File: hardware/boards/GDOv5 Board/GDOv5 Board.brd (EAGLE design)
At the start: 34 x 53.6 mm, 29 parts, among them IC1 DS1820, IC2 3.3V REG, J1 DCJ0202, Q1 BSS84, Q2 BSS138, Q3 BSS138

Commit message: Fixing Board issues
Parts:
- added Q4: IRLML2502, bss138_10:SOT23
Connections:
- new net N$1: J1.3, Q4.3
- net +5V: now also J1.1, Q4.1; no longer J1.3
- net GND: now also Q4.2; no longer J1.1
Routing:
- net +5V: track 49.1 -> 54.1 mm
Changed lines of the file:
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@@
 <layers>
 <layer number="1" name="Top" color="4" fill="1" visible="yes" active="yes"/>
-<layer number="16" name="Bottom" color="1" fill="1" visible="yes" active="yes"/>
+<layer number="16" name="Bottom" color="1" fill="1" visible="no" active="yes"/>
 <layer number="17" name="Pads" color="2" fill="1" visible="yes" active="yes"/>
 <layer number="18" name="Vias" color="2" fill="1" visible="yes" active="yes"/>
@@
 <layer number="20" name="Dimension" color="15" fill="1" visible="yes" active="yes"/>
 <layer number="21" name="tPlace" color="7" fill="1" visible="yes" active="yes"/>
-<layer number="22" name="bPlace" color="7" fill="1" visible="yes" active="yes"/>
+<layer number="22" name="bPlace" color="7" fill="1" visible="no" active="yes"/>
 <layer number="23" name="tOrigins" color="15" fill="1" visible="yes" active="yes"/>
-<layer number="24" name="bOrigins" color="15" fill="1" visible="yes" active="yes"/>
+<layer number="24" name="bOrigins" color="15" fill="1" visible="no" active="yes"/>
 <layer number="25" name="tNames" color="7" fill="1" visible="yes" active="yes"/>
-<layer number="26" name="bNames" color="7" fill="1" visible="yes" active="yes"/>
+<layer number="26" name="bNames" color="7" fill="1" visible="no" active="yes"/>
 <layer number="27" name="tValues" color="7" fill="1" visible="yes" active="yes"/>
 <layer number="28" name="bValues" color="7" fill="1" visible="yes" active="yes"/>
@@
 </element>
 <element name="S1" library="SparkFun-Electromechanical" package="TACTILE-SWITCH-1101NE" value="RESET-SWITCH" x="30.48" y="43.18" rot="R270"/>
+<element name="Q4" library="bss138_10" package="SOT23" value="IRLML2502" x="3.81" y="36.83">
+<attribute name="MPN" value="BSS138" x="3.81" y="36.83" size="1.778" layer="27" display="off"/>
+<attribute name="OC_NEWARK" value="67R2009" x="3.81" y="36.83" size="1.778" layer="27" display="off"/>
+<attribute name="OC_FARNELL" value="9845330" x="3.81" y="36.83" size="1.778" layer="27" display="off"/>
+<attribute name="MF" value="Fairchild" x="3.81" y="36.83" size="1.778" layer="27" display="off"/>
+</element>
 </elements>
 <signals>
@@
 <contactref element="C9" pad="C"/>
 <contactref element="C4" pad="2"/>
-<contactref element="J1" pad="1"/>
 <contactref element="R9" pad="1"/>
 <contactref element="R10" pad="1"/>
@@
 <wire x1="6.4008" y1="76.8096" x2="6.35" y2="76.835" width="0.1524" layer="1"/>
 <via x="9.144" y="52.7304" extent="1-16" drill="0.3302"/>
+<contactref element="Q4" pad="2"/>
+<wire x1="10.795" y1="28.2575" x2="4.76" y2="35.83" width="0" layer="19" extent="1-1"/>
 </signal>
 <signal name="+5V">
 <contactref element="IC2" pad="3"/>
 <contactref element="C8" pad="A"/>
-<contactref element="J1" pad="3"/>
 <wire x1="22.2504" y1="68.7324" x2="24.5364" y2="71.0184" width="0.1524" layer="1"/>
 <wire x1="24.5364" y1="71.0184" x2="24.635" y2="71.12" width="0.1524" layer="1"/>
@@
 <wire x1="2.4384" y1="52.7304" x2="3.6576" y2="53.9496" width="0.1524" layer="1"/>
 <wire x1="2.4384" y1="49.53" x2="2.4384" y2="52.7304" width="0.1524" layer="1"/>
-<wire x1="1.0668" y1="48.1584" x2="2.4384" y2="49.53" width="0.1524" layer="1"/>
-<wire x1="1.0668" y1="43.1292" x2="1.0668" y2="48.1584" width="0.1524" layer="1"/>
-<wire x1="7.0104" y1="37.1856" x2="1.0668" y2="43.1292" width="0.1524" layer="1"/>
 <wire x1="22.098" y1="68.58" x2="22.1996" y2="68.6689" width="0.1524" layer="1"/>
-<wire x1="7.0104" y1="37.1856" x2="7.16" y2="37.1475" width="0.1524" layer="1"/>
+<contactref element="J1" pad="1"/>
+<wire x1="12.54125" y1="37.1475" x2="13.26" y2="37.1475" width="0.1524" layer="1"/>
+<wire x1="2.54" y1="43.33875" x2="12.54125" y2="37.1475" width="0.1524" layer="1"/>
+<wire x1="1.42875" y1="43.33875" x2="2.54" y2="43.33875" width="0.1524" layer="1"/>
+<wire x1="1.11125" y1="43.65625" x2="1.42875" y2="43.33875" width="0.1524" layer="1"/>
+<wire x1="1.11125" y1="48.26" x2="1.11125" y2="43.65625" width="0.1524" layer="1"/>
+<wire x1="2.38125" y1="49.53" x2="1.11125" y2="48.26" width="0.1524" layer="1"/>
+<wire x1="2.38125" y1="49.53" x2="2.4384" y2="49.53" width="0.1524" layer="1"/>
+<contactref element="Q4" pad="1"/>
+<wire x1="2.86" y1="35.83" x2="1.42875" y2="43.33875" width="0" layer="19" extent="1-1"/>
 </signal>
 <signal name="+3.3V">
@@
 <wire x1="21.9456" y1="58.5216" x2="21.91" y2="58.59" width="0.1524" layer="1"/>
 </signal>
+<signal name="N$1">
+<contactref element="J1" pad="3"/>
+<contactref element="Q4" pad="3"/>
+<wire x1="3.81" y1="37.83" x2="7.16" y2="37.1475" width="0" layer="19" extent="1-1"/>
+</signal>
 </signals>

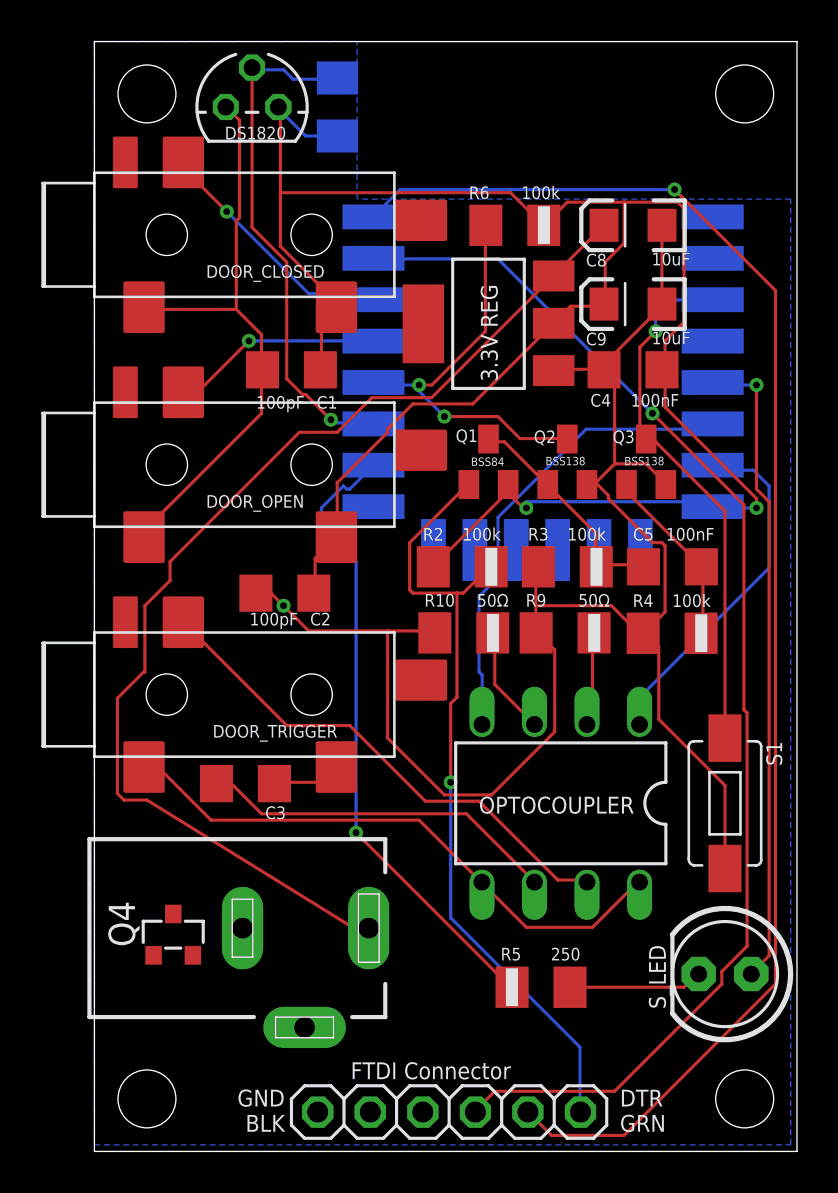
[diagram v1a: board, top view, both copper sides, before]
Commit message: Updating board to better match prototype design
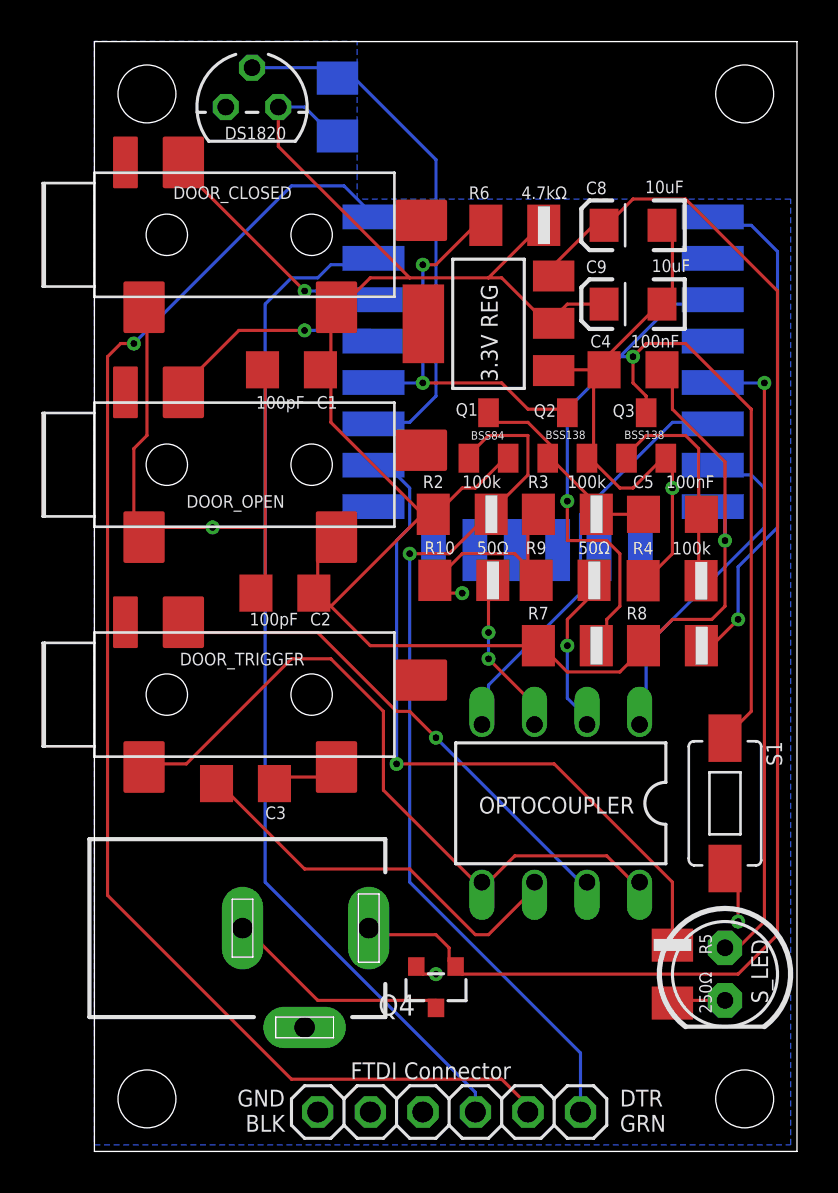
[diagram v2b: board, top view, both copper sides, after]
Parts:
- added R7: 4.7kΩ, resistor:M3216
- added R8: 10k, resistor:M3216
- R5: value 250 -> 250Ω
- R6: value 100k -> 4.7kΩ
- moved Q4 13.0 mm to (16.5, 34.3), turned to 180 degrees
- moved R5 6.38 mm to (27.9, 34.9), turned to 90 degrees
- moved R10 2.54 mm to (17.9, 54.0)
- moved R9 2.54 mm to (22.8, 54.0)
- moved C5 2.54 mm to (27.9, 57.1)
- moved R2 2.54 mm to (17.8, 57.1)
- moved R3 2.54 mm to (22.9, 57.1)
- moved R4 2.54 mm to (27.9, 53.9)
- moved Q1 1.27 mm to (19.1, 61.0)
- moved Q2 1.27 mm to (22.9, 61.0)
- moved Q3 1.27 mm to (26.7, 61.0)
- turned S_LED to 270 degrees
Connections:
- net +3.3V: now also R7.1, R8.1
- net ENABLE: now also R7.2
- net RESET: now also R8.2
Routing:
- net GND: track 111.1 -> 73.2 mm, vias 1 -> 5
- net ENABLE: track 25.7 -> 51.0 mm, vias 1 -> 2
- net RESET: track 0.00 -> 24.7 mm, vias 0 -> 1
- net +5V: track 54.1 -> 67.6 mm
- net RXD: track 61.1 -> 49.5 mm, vias 1 -> 0
- net N$1: track 0.00 -> 11.1 mm
- net CTRL-: track 28.1 -> 33.9 mm
- net DTR: track 38.6 -> 43.1 mm
- net ARD15: track 30.5 -> 34.6 mm
- net +3.3V: track 101.9 -> 98.0 mm, vias 2 -> 1
- net N$4: track 6.48 -> 2.67 mm
- net N$6: track 4.58 -> 8.34 mm, vias 0 -> 1
- net TXD: track 71.0 -> 67.8 mm
- net N$7: track 5.28 -> 8.11 mm, vias 0 -> 2
- net N$3: track 17.4 -> 20.1 mm
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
